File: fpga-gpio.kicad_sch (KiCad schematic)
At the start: 11 parts, among them Q5 DMG1012T-7, Q7 DMG1012T-7, Q8 DMG1012T-7, U1 MPFS250T-FCVG484

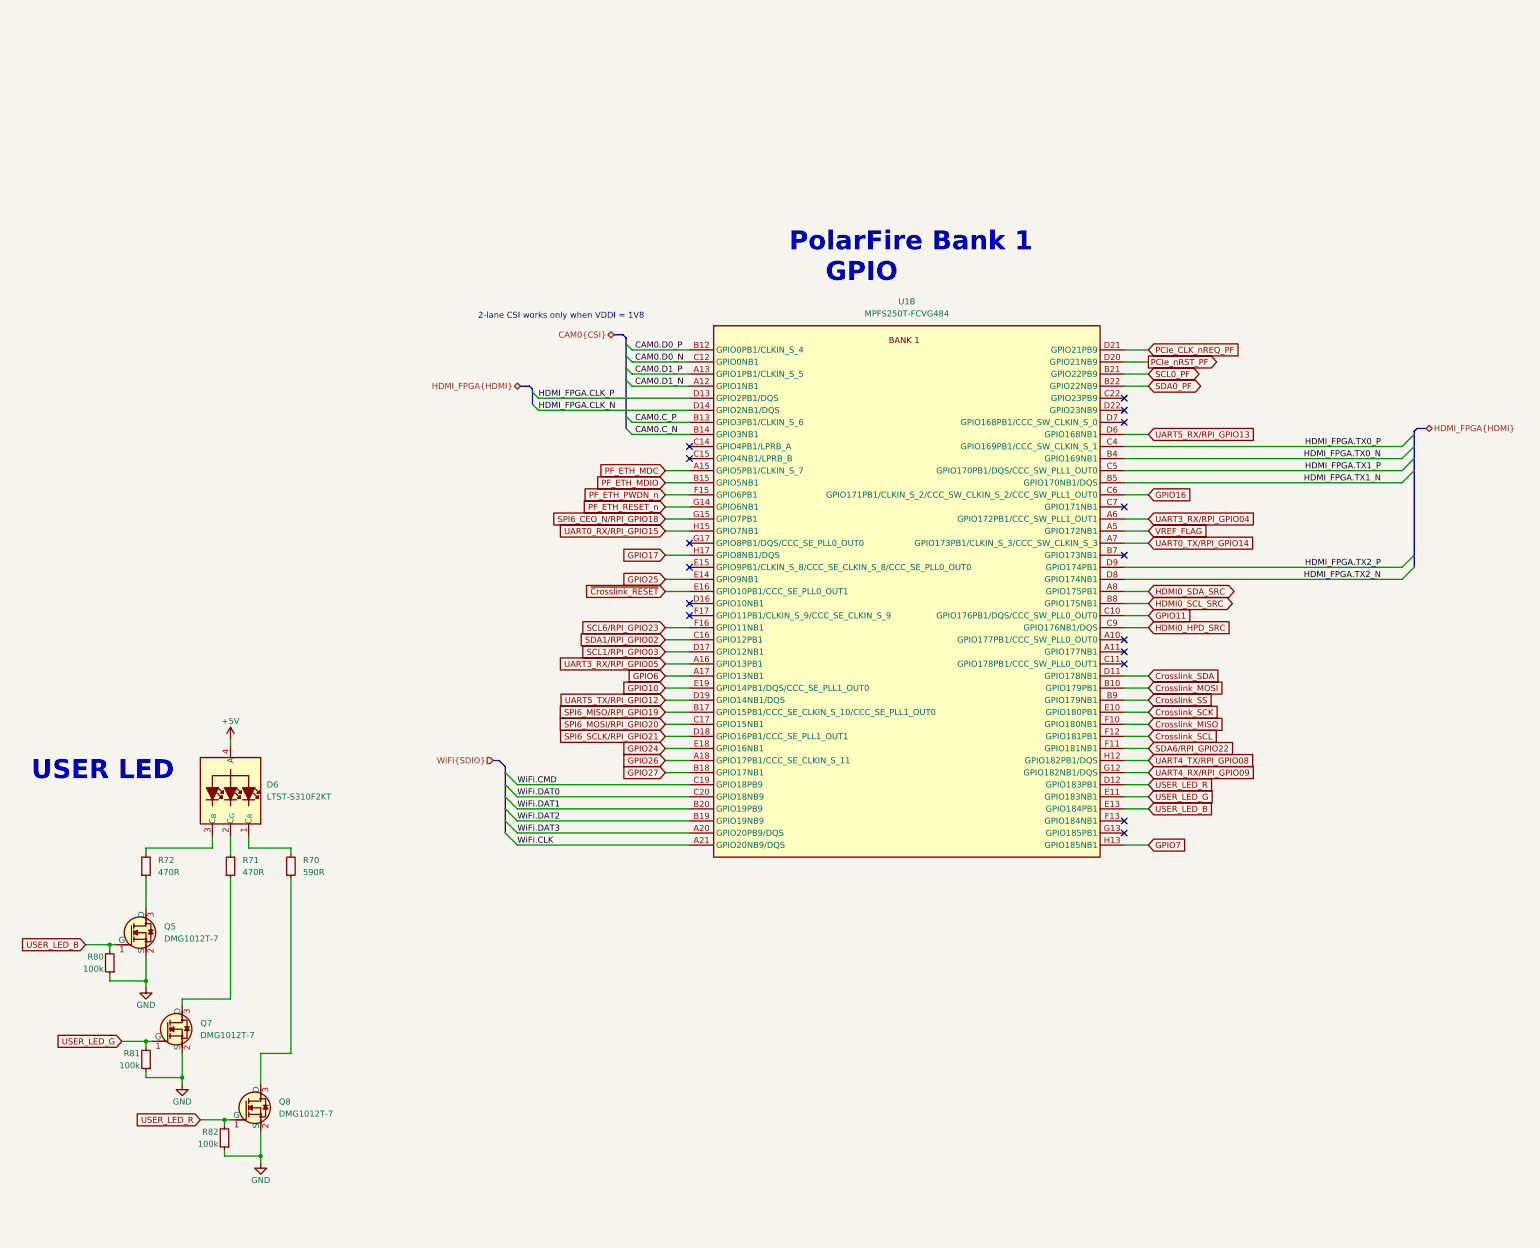
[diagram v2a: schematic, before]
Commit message: [#57505] Start moving logic level converters to GPIO sheet
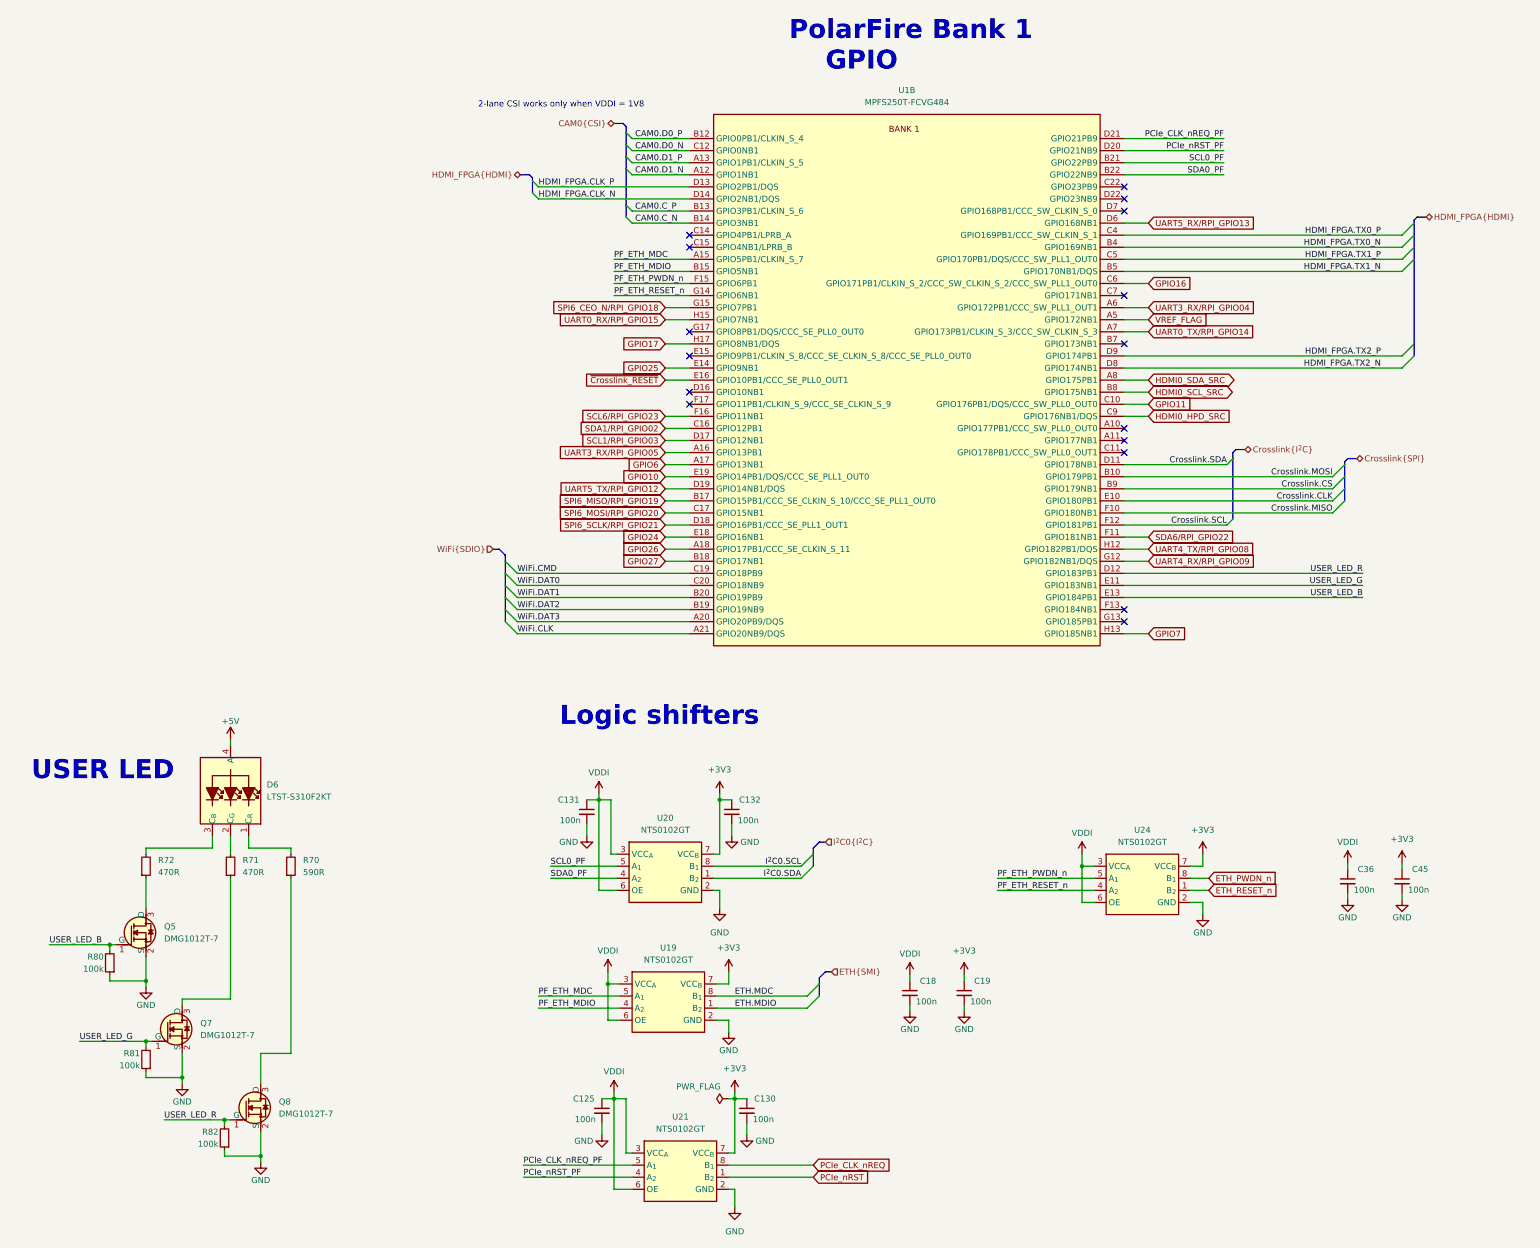
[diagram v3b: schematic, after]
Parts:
- added C125, C130, C131, C132, C18, C19, C36, C45: C_100n_0402, antmicro-footprints:C_0402_1005Metric, symbol antmicroCapacitors0402:C_100n_0402
- added U19, U20, U21, U24: NTS0102_XSON, antmicro-footprints:XSON-8_1x1.95mm_P0.5mm, symbol antmicroLogicTranslatorsLevelShifters:NTS0102_XSON
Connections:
- net GND: now also C125.2, C130.2, C131.2, C132.2, C18.2, C19.2, C36.2, C45.2, U19.2 (GND), U20.2 (GND), U21.2 (GND), U24.2 (GND)
- net PCIe_CLK_nREQ_PF: now also U21.5 (A_{1})
- net PCIe_nRST_PF: now also U21.4 (A_{2})
- net PF_ETH_MDC: now also U19.5 (A_{1})
- net PF_ETH_MDIO: now also U19.4 (A_{2})
- net PF_ETH_PWDN_n: now also U24.5 (A_{1})
- net PF_ETH_RESET_n: now also U24.4 (A_{2})
- net SCL0_PF: now also U20.5 (A_{1})
- net SDA0_PF: now also U20.4 (A_{2})
- net Crosslink_MISO renamed Crosslink.MISO
- net Crosslink_MOSI renamed Crosslink.MOSI
- net Crosslink_SCK renamed Crosslink.CLK
- net Crosslink_SCL renamed Crosslink.SCL
- net Crosslink_SDA renamed Crosslink.SDA
- net Crosslink_SS renamed Crosslink.CS
- new net +3V3: C130.1, C132.1, C19.1, C45.1, U19.7 (VCC_{B}), U20.7 (VCC_{B}), U21.7 (VCC_{B}), U24.7 (VCC_{B})
- new net ETH.MDC: U19.8 (B_{1})
- new net ETH.MDIO: U19.1 (B_{2})
- new net ETH_PWDN_n: U24.8 (B_{1})
- new net ETH_RESET_n: U24.1 (B_{2})
- new net I^{2}C0.SCL: U20.8 (B_{1})
- new net I^{2}C0.SDA: U20.1 (B_{2})
- new net PCIe_CLK_nREQ: U21.8 (B_{1})
- new net PCIe_nRST: U21.1 (B_{2})
- new net VDDI: C125.1, C131.1, C18.1, C36.1, U19.3 (VCC_{A}), U19.6 (OE), U20.3 (VCC_{A}), U20.6 (OE), U21.3 (VCC_{A}), U21.6 (OE), U24.3 (VCC_{A}), U24.6 (OE)
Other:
- note added: "Logic shifters"
- moved on the sheet: U1B

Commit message: [#57505] Finish migration to hierarchical structure
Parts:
- added C123, C178, C218, C81: C_100n_0402, antmicro-footprints:C_0402_1005Metric, symbol antmicroCapacitors0402:C_100n_0402
- added U14, U25, U27, U29: NTS0102_XSON, antmicro-footprints:XSON-8_1x1.95mm_P0.5mm, symbol antmicroLogicTranslatorsLevelShifters:NTS0102_XSON
- added U18: 74LVC1T45GM, antmicro-footprints:SOT-886, symbol antmicroLogicTranslatorsLevelShifters:74LVC1T45GM
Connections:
- net +3V3: now also C125.1, C131.1, C218.1, C81.1, U14.7 (VCC_{B}), U18.6 (VCCB), U25.7 (VCC_{B}), U27.7 (VCC_{B}), U29.7 (VCC_{B}); no longer C130.1, C132.1
- net GND: now also C123.2, C178.2, C218.2, C81.2, U14.2 (GND), U18.2 (GND), U18.5 (DIR), U25.2 (GND), U27.2 (GND), U29.2 (GND)
- net HDMI0_HPD_SRC: now also U18.3 (A)
- net HDMI0_SCL_SRC: now also U14.4 (A_{2})
- net HDMI0_SDA_SRC: now also U14.5 (A_{1})
- net VDDI: now also C130.1, C132.1, C123.1, C178.1, U14.3 (VCC_{A}), U14.6 (OE), U18.1 (VCCA), U25.3 (VCC_{A}), U25.6 (OE), U27.3 (VCC_{A}), U27.6 (OE), U29.3 (VCC_{A}), U29.6 (OE); no longer C125.1, C131.1
- net WiFi.CLK: now also U29.1 (B_{2}); no longer U1.A21 (GPIO20NB9/DQS)
- net WiFi.CMD: now also U25.8 (B_{1}); no longer U1.C19 (GPIO18PB9)
- net WiFi.DAT0: now also U27.8 (B_{1}); no longer U1.C20 (GPIO18NB9)
- net WiFi.DAT1: now also U25.1 (B_{2}); no longer U1.B20 (GPIO19PB9)
- net WiFi.DAT2: now also U29.8 (B_{1}); no longer U1.B19 (GPIO19NB9)
- net WiFi.DAT3: now also U27.1 (B_{2}); no longer U1.A20 (GPIO20PB9/DQS)
- new net PI3HDX511F.SDA: U14.8 (B_{1})
- new net PI3HDX511F_HOTPLUG: U18.4 (B)
- new net PI3HDX511F_SCL: U14.1 (B_{2})
- new net WiFi_CLK: U1.A21 (GPIO20NB9/DQS), U29.4 (A_{2})
- new net WiFi_CMD: U1.C19 (GPIO18PB9), U25.5 (A_{1})
- new net WiFi_DATA_0: U1.C20 (GPIO18NB9), U27.5 (A_{1})
- new net WiFi_DATA_1: U1.B20 (GPIO19PB9), U25.4 (A_{2})
- new net WiFi_DATA_2: U1.B19 (GPIO19NB9), U29.5 (A_{1})
- new net WiFi_DATA_3: U1.A20 (GPIO20PB9/DQS), U27.4 (A_{2})
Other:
- note added: "Level shifters"
- moved on the sheet: C125, C130, C131, C132

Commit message: [#57422] Clean DRC
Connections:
- net PI3HDX511F_SCL renamed PI3HDX511F.SCL
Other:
- note removed: "Level shifters"
- moved on the sheet: C123, C125, C130, C131, C132, C178, C18, C19, C218, C36, C45, C81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

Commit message: [#57422] Finishing touches
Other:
- moved on the sheet: C125, C130, C131, C132, C178, C18, C19, C218, C36, C45, D6, Q5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

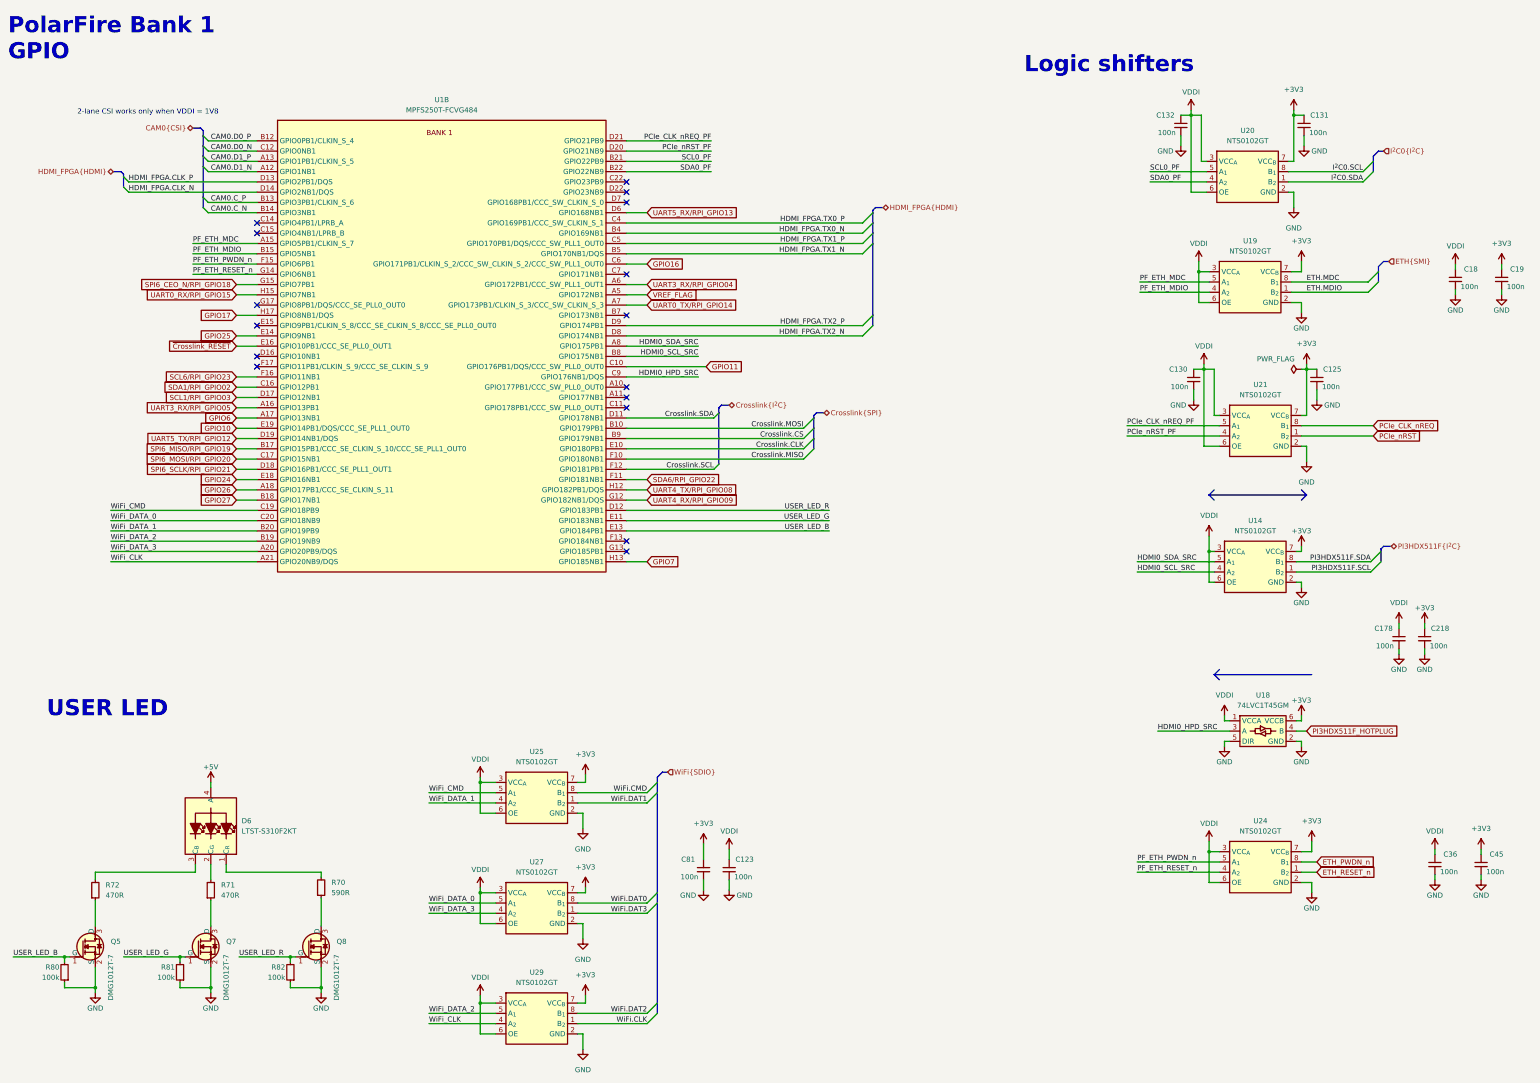
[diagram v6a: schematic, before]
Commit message: [#57422] Align schematics
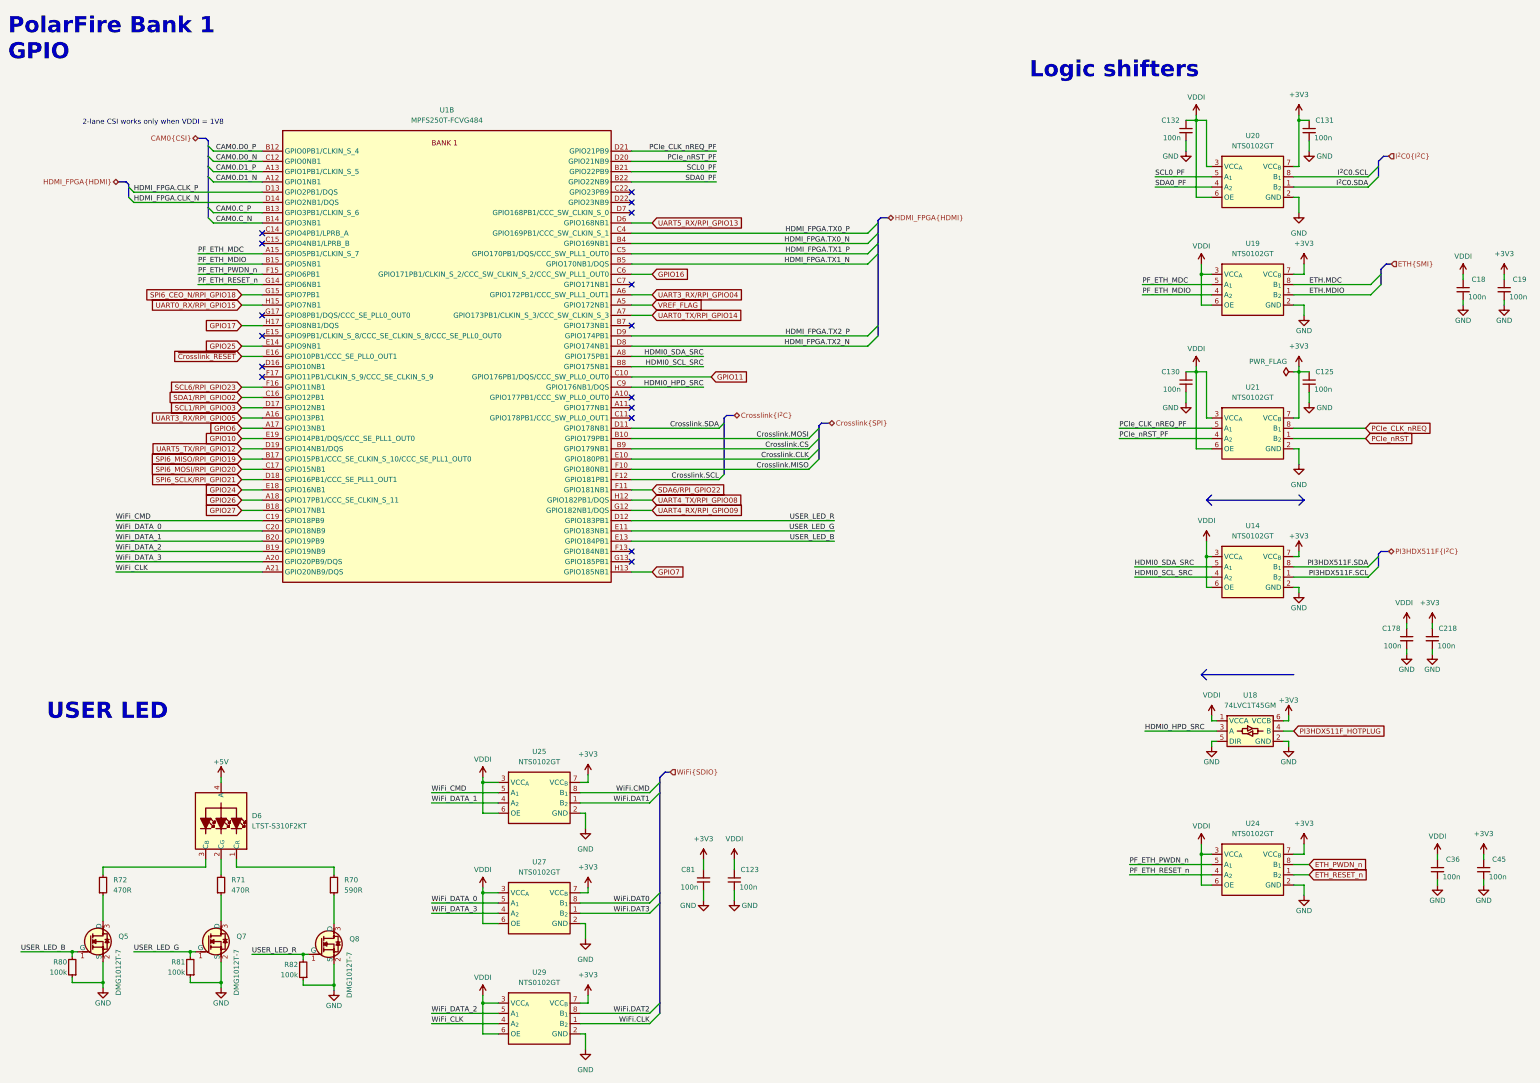
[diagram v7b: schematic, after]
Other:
- moved on the sheet: C123, C125, C130, C131, C132, C178, C18, C19, C218, C36, C45, C81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

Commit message: [#59446] Add Q5-Q8 to BOM
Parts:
- Q5, Q7, Q8: now in the parts list
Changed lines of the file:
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@@
   )
   (symbol (lib_id "antmicroTransistorsFETsMOSFETsSingle:DMG1012T-7") (at 87.63 247.015 0) (unit 1)
-    (in_bom no) (on_board yes) (dnp no)
+    (in_bom yes) (on_board yes) (dnp no)
     (property "Reference" "Q8" (at 97.79 243.205 0)
       (effects (font (size 1.27 1.27) (thickness 0.15)) (justify left))
@@
   )
   (symbol (lib_id "antmicroTransistorsFETsMOSFETsSingle:DMG1012T-7") (at 59.69 246.38 0) (unit 1)
-    (in_bom no) (on_board yes) (dnp no)
+    (in_bom yes) (on_board yes) (dnp no)
     (property "Reference" "Q7" (at 69.85 242.57 0)
       (effects (font (size 1.27 1.27) (thickness 0.15)) (justify left))
@@
   )
   (symbol (lib_id "antmicroTransistorsFETsMOSFETsSingle:DMG1012T-7") (at 30.48 246.38 0) (unit 1)
-    (in_bom no) (on_board yes) (dnp no)
+    (in_bom yes) (on_board yes) (dnp no)
     (property "Reference" "Q5" (at 40.64 242.57 0)
       (effects (font (size 1.27 1.27) (thickness 0.15)) (justify left))
